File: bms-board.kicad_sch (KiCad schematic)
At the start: 1 part, among them U1 LTC6804-2

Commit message: Release/0.1 (#8)
* feat: add 6804-2 kicad symbol

* feat: add 6804-2 kicad symbol (#3)

* TEMPLATE: add pull request description template

* feat: add automated git flow setup script

* update feature/add-cells branch to latest develop edition (#4)

* feat: add 6804-2 kicad symbol

* TEMPLATE: add pull request description template

* feat: add automated git flow setup script

* update feature/our-symbol-library branch to latest develop edition (#5)

* TEMPLATE: add pull request description template

* feat: add automated git flow setup script

* feat: a maybe working fixed wing schematic symbol library

* feat: add line to checkout dev branch when running setup script

* feat: fix FixedWing symbol library to include LTC6804-2

* refactor: verifying symbol library works, remove individual ltc6804-2 symbol

* feat: adding needed files

* feat: edit conflict in setup script

* Merging new develop into new feature (#6)

* feat: add 6804-2 kicad symbol

* TEMPLATE: add pull request description template

* feat: add automated git flow setup script

* update feature/our-symbol-library branch to latest develop edition (#5)

* TEMPLATE: add pull request description template

* feat: add automated git flow setup script

* feat: a maybe working fixed wing schematic symbol library

* feat: add line to checkout dev branch when running setup script

* feat: fix FixedWing symbol library to include LTC6804-2

* refactor: verifying symbol library works, remove individual ltc6804-2 symbol

* feat: adding needed files

* feat: edit conflict in setup script

---------

Co-authored-by: Ephram Cola Jacquin <89238547+ephram2004@users.noreply.github.com>
Co-authored-by: Ephram Cola Jacquin <ecolajacquin@gmail.com>

* fix: changed symbol for easier schematic design and orginization by pin logic

* docs: Update pull_request_template.md

---------

Co-authored-by: Ephram Cola Jacquin <89238547+ephram2004@users.noreply.gith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
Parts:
- removed U1: LTC6804-2, Package_SO:SSOP-48_5.3x12.8mm_P0.5mm, symbol Battery_Management:LTC6804-2
- added U3: LTC6804-2, Package_SO:SSOP-48_5.3x12.8mm_P0.5mm, symbol FixedWing:LTC6804-2
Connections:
- new net: U3.30 (V-), U3.31 (V-)
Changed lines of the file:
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@@
 (kicad_sch (version 20230121) (generator eeschema)
   (paper "A4")
-  (symbol (lib_id "Battery_Management:LTC6804-2") (at 148.59 92.71 0) (unit 1)
+  (symbol (lib_name "LTC6804-2_1") (lib_id "FixedWing:LTC6804-2") (at 133.35 96.52 0) (unit 1)
     (in_bom yes) (on_board yes) (dnp no) (fields_autoplaced)
-    (property "Reference" "U1" (at 148.59 54.61 0)
-      (effects (font (size 1.27 1.27)))
+    (property "Reference" "U3" (at 135.5441 58.42 0)
+      (effects (font (size 1.27 1.27)) (justify left))
     )
-    (property "Value" "LTC6804-2" (at 148.59 57.15 0)
-      (effects (font (size 1.27 1.27)))
+    (property "Value" "LTC6804-2" (at 135.5441 60.96 0)
+      (effects (font (size 1.27 1.27)) (justify left))
     )
-    (property "Footprint" "Package_SO:SSOP-48_5.3x12.8mm_P0.5mm" (at 148.59 130.81 0)
+    (property "Footprint" "Package_SO:SSOP-48_5.3x12.8mm_P0.5mm" (at 133.35 133.35 0)
       (effects (font (size 1.27 1.27)) hide)
     )
-    (property "Datasheet" "https://www.analog.com/media/en/technical-documentation/data-sheets/680412fc.pdf" (at 151.13 55.88 0)
+    (property "Datasheet" "https://www.analog.com/media/en/technical-documentation/data-sheets/680412fc.pdf" (at 147.32 62.23 0)
       (effects (font (size 1.27 1.27)) hide)
     )
+    (pin "37")
+    (pin "2")
+    (pin "39")
+    (pin "32")
+    (pin "36")
+    (pin "4")
+    (pin "41")
+    (pin "11")
+    (pin "20")
+    (pin "12")
+    (pin "21")
+    (pin "30")
+    (pin "33")
+    (pin "16")
     (pin "19")
-    (pin "20")
+    (pin "34")
+    (pin "40")
+    (pin "1")
+    (pin "13")
     (pin "17")
-    (pin "21")
-    (pin "39")
-    (pin "40")
-    (pin "16")
+    (pin "10")
+    (pin "18")
+    (pin "22")
+    (pin "26")
+    (pin "23")
+    (pin "24")
+    (pin "28")
     (pin "15")
-    (pin "22")
-    (pin "12")
-    (pin "44")
+    (pin "14")
+    (pin "27")
+    (pin "25")
+    (pin "29")
+    (pin "3")
+    (pin "35")
+    (pin "31")
+    (pin "38")
+    (pin "5")
+    (pin "42")
+    (pin "43")
+    (pin "48")
+    (pin "6")
+    (pin "7")
     (pin "45")
+    (pin "8")
+    (pin "9")
     (pin "46")
     (pin "47")
-    (pin "48")
-    (pin "23")
-    (pin "4")
-    (pin "11")
-    (pin "10")
-    (pin "5")
-    (pin "6")
-    (pin "7")
-    (pin "8")
-    (pin "9")
-    (pin "1")
-    (pin "24")
-    (pin "25")
-    (pin "26")
-    (pin "27")
-    (pin "28")
-    (pin "29")
-    (pin "3")
-    (pin "30")
-    (pin "31")
-    (pin "32")
-    (pin "33")
-    (pin "34")
-    (pin "35")
-    (pin "36")
-    (pin "37")
-    (pin "38")
-    (pin "13")
-    (pin "18")
-    (pin "2")
-    (pin "14")
-    (pin "41")
-    (pin "42")
-    (pin "43")
+    (pin "44")
     (instances
       (project "bms-board"
         (path "/8a7831d1-a913-4f04-8780-225d2234b41d"
-          (reference "U1") (unit 1)
+          (reference "U3") (unit 1)
         )
       )

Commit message: feat: started adding cell nets
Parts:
- removed U3: LTC6804-2, Package_SO:SSOP-48_5.3x12.8mm_P0.5mm, symbol FixedWing:LTC6804-2
- added U1: LTC6804-2, Package_SO:SSOP-48_5.3x12.8mm_P0.5mm, symbol FixedWing:LTC6804-2
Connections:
- new net: U1.14 (C6), U1.16 (C5), U1.18 (C4)
- new net: U1.2 (C12), U1.4 (C11), U1.6 (C10)
- new net: U1.30 (V-), U1.31 (V-)
- new net C0_IN: U1.26 (C0)
- no-connect marks 0 -> 6
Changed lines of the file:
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@@
 (kicad_sch (version 20230121) (generator eeschema)
   (paper "A4")
-  (symbol (lib_name "LTC6804-2_1") (lib_id "FixedWing:LTC6804-2") (at 133.35 96.52 0) (unit 1)
+  (junction (at 158.75 62.23) (diameter 0) (color 0 0 0 0)
+  )
+  (junction (at 158.75 92.71) (diameter 0) (color 0 0 0 0)
+  )
+  (no_connect (at 154.94 64.77))
+  (no_connect (at 154.94 90.17))
+  (no_connect (at 154.94 95.25))
+  (no_connect (at 154.94 69.85))
+  (no_connect (at 154.94 100.33))
+  (no_connect (at 154.94 59.69))
+  (wire (pts (xy 154.94 57.15) (xy 158.75 57.15))
+    (stroke (width 0) (type default))
+  )
+  (wire (pts (xy 158.75 57.15) (xy 158.75 62.23))
+    (stroke (width 0) (type default))
+  )
+  (wire (pts (xy 158.75 92.71) (xy 158.75 97.79))
+    (stroke (width 0) (type default))
+  )
+  (wire (pts (xy 154.94 67.31) (xy 158.75 67.31))
+    (stroke (width 0) (type default))
+  )
+  (wire (pts (xy 154.94 62.23) (xy 158.75 62.23))
+    (stroke (width 0) (type default))
+  )
+  (wire (pts (xy 158.75 87.63) (xy 158.75 92.71))
+    (stroke (width 0) (type default))
+  )
+  (wire (pts (xy 154.94 97.79) (xy 158.75 97.79))
+    (stroke (width 0) (type default))
+  )
+  (wire (pts (xy 144.78 125.73) (xy 144.78 123.19))
+    (stroke (width 0) (type default))
+  )
+  (wire (pts (xy 154.94 92.71) (xy 158.75 92.71))
+    (stroke (width 0) (type default))
+  )
+  (wire (pts (xy 154.94 87.63) (xy 158.75 87.63))
+    (stroke (width 0) (type default))
+  )
+  (wire (pts (xy 154.94 118.11) (xy 203.2 118.11))
+    (stroke (width 0) (type default))
+  )
+  (wire (pts (xy 139.7 125.73) (xy 139.7 123.19))
+    (stroke (width 0) (type default))
+  )
+  (wire (pts (xy 158.75 62.23) (xy 158.75 67.31))
+    (stroke (width 0) (type default))
+  )
+  (wire (pts (xy 139.7 125.73) (xy 144.78 125.73))
+    (stroke (width 0) (type default))
+  )
+  (global_label "C1_IN" (shape input) (at 203.2 113.03 0) (fields_autoplaced)
+    (effects (font (size 1.27 1.27)) (justify left))
+    (property "Intersheetrefs" "${INTERSHEET_REFS}" (at 211.5676 113.03 0)
+      (effects (font (size 1.27 1.27)) (justify left) hide)
+    )
+  )
+  (global_label "C0_IN" (shape input) (at 203.2 118.11 0) (fields_autoplaced)
+    (effects (font (size 1.27 1.27)) (justify left))
+    (property "Intersheetrefs" "${INTERSHEET_REFS}" (at 211.5676 118.11 0)
+      (effects (font (size 1.27 1.27)) (justify left) hide)
+    )
+  )
+  (global_label "C2_IN" (shape input) (at 203.2 107.95 0) (fields_autoplaced)
+    (effects (font (size 1.27 1.27)) (justify left))
+    (property "Intersheetrefs" "${INTERSHEET_REFS}" (at 211.5676 107.95 0)
+      (effects (font (size 1.27 1.27)) (justify left) hide)
+    )
+  )
+  (global_label "C5_IN" (shape input) (at 203.2 82.55 0) (fields_autoplaced)
+    (effects (font (size 1.27 1.27)) (justify left))
+    (property "Intersheetrefs" "${INTERSHEET_REFS}" (at 211.5676 82.55 0)
+      (effects (font (size 1.27 1.27)) (justify left) hide)
+    )
+  )
+  (global_label "C6_IN" (shape input) (at 203.2 77.47 0) (fields_autoplaced)
+    (effects (font (size 1.27 1.27)) (justify left))
+    (property "Intersheetrefs" "${INTERSHEET_REFS}" (at 211.5676 77.47 0)
+      (effects (font (size 1.27 1.27)) (justify left) hide)
+    )
+  )
+  (global_label "C4_IN" (shape input) (at 203.2 87.63 0) (fields_autoplaced)
+    (effects (font (size 1.27 1.27)) (justify left))
+    (property "Intersheetrefs" "${INTERSHEET_REFS}" (at 211.5676 87.63 0)
+      (effects (font (size 1.27 1.27)) (justify left) hide)
+    )
+  )
+  (global_label "C7_IN" (shape input) (at 203.2 72.39 0) (fields_autoplaced)
+    (effects (font (size 1.27 1.27)) (justify left))
+    (property "Intersheetrefs" "${INTERSHEET_REFS}" (at 211.5676 72.39 0)
+      (effects (font (size 1.27 1.27)) (justify left) hide)
+    )
+  )
+  (global_label "C3_IN" (shape input) (at 203.2 102.87 0) (fields_autoplaced)
+    (effects (font (size 1.27 1.27)) (justify left))
+    (property "Intersheetrefs" "${INTERSHEET_REFS}" (at 211.5676 102.87 0)
+      (effects (font (size 1.27 1.27)) (justify left) hide)
+    )
+  )
+  (symbol (lib_name "LTC6804-2_1") (lib_id "FixedWing:LTC6804-2") (at 142.24 87.63 0) (unit 1)
     (in_bom yes) (on_board yes) (dnp no) (fields_autoplaced)
-    (property "Reference" "U3" (at 135.5441 58.42 0)
+    (property "Reference" "U1" (at 144.4341 49.53 0)
       (effects (font (size 1.27 1.27)) (justify left))
     )
-    (property "Value" "LTC6804-2" (at 135.5441 60.96 0)
+    (property "Value" "LTC6804-2" (at 144.4341 52.07 0)
       (effects (font (size 1.27 1.27)) (justify left))
     )
-    (property "Footprint" "Package_SO:SSOP-48_5.3x12.8mm_P0.5mm" (at 133.35 133.35 0)
+    (property "Footprint" "Package_SO:SSOP-48_5.3x12.8mm_P0.5mm" (at 142.24 124.46 0)
       (effects (font (size 1.27 1.27)) hide)
     )
-    (property "Datasheet" "https://www.analog.com/media/en/technical-documentation/data-sheets/680412fc.pdf" (at 147.32 62.23 0)
+    (property "Datasheet" "https://www.analog.com/media/en/technical-documentation/data-sheets/680412fc.pdf" (at 156.21 53.34 0)
       (effects (font (size 1.27 1.27)) hide)
     )
+    (pin "31")
+    (pin "36")
     (pin "37")
+    (pin "18")
+    (pin "48")
+    (pin "5")
+    (pin "6")
+    (pin "23")
+    (pin "1")
+    (pin "34")
+    (pin "10")
+    (pin "26")
+    (pin "22")
+    (pin "29")
+    (pin "32")
+    (pin "14")
+    (pin "16")
     (pin "2")
+    (pin "44")
+    (pin "11")
+    (pin "42")
+    (pin "7")
+    (pin "8")
+    (pin "9")
+    (pin "17")
+    (pin "24")
     (pin "39")
-    (pin "32")
-    (pin "36")
-    (pin "4")
-    (pin "41")
-    (pin "11")
+    (pin "21")
+    (pin "43")
+    (pin "19")
+    (pin "40")
+    (pin "35")
+    (pin "30")
+    (pin "45")
+    (pin "15")
+    (pin "25")
+    (pin "28")
+    (pin "46")
+    (pin "38")
     (pin "20")
     (pin "12")
-    (pin "21")
-    (pin "30")
+    (pin "3")
+    (pin "41")
+    (pin "4")
     (pin "33")
-    (pin "16")
-    (pin "19")
-    (pin "34")
-    (pin "40")
-    (pin "1")
     (pin "13")
-    (pin "17")
-    (pin "10")
-    (pin "18")
-    (pin "22")
-    (pin "26")
-    (pin "23")
-    (pin "24")
-    (pin "28")
-    (pin "15")
-    (pin "14")
     (pin "27")
-    (pin "25")
-    (pin "29")
-    (pin "3")
-    (pin "35")
-    (pin "31")
-    (pin "38")
-    (pin "5")
-    (pin "42")
-    (pin "43")
-    (pin "48")
-    (pin "6")
-    (pin "7")
-    (pin "45")
-    (pin "8")
-    (pin "9")
-    (pin "46")
     (pin "47")
-    (pin "44")
     (instances
       (project "bms-board"
         (path "/8a7831d1-a913-4f04-8780-225d2234b41d"
-          (reference "U3") (unit 1)
+          (reference "U1") (unit 1)
         )
       )

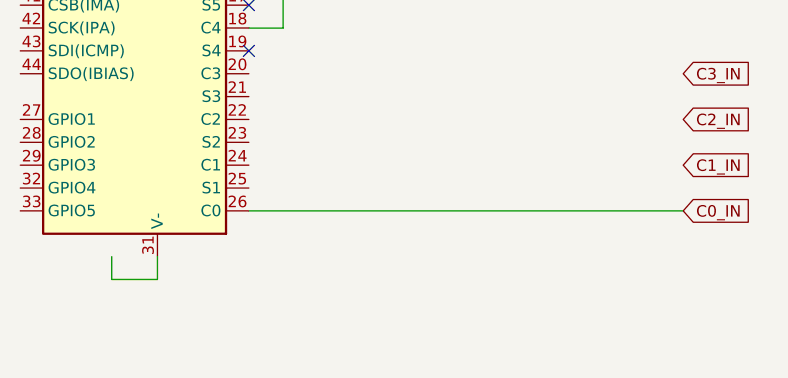
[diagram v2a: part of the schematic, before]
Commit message: feat: still some more LTC6804-2 symbol edits
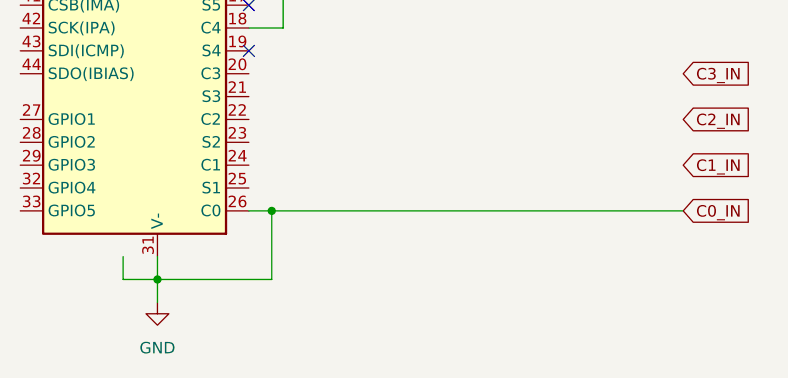
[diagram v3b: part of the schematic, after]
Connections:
- net C0_IN is gone; now on net GND: U1.26 (C0)
- net GND: now reaches U1.30 (V-), U1.31 (V-)
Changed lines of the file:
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@@
   (junction (at 158.75 62.23) (diameter 0) (color 0 0 0 0)
   )
+  (junction (at 157.48 118.11) (diameter 0) (color 0 0 0 0)
+  )
   (junction (at 158.75 92.71) (diameter 0) (color 0 0 0 0)
+  )
+  (junction (at 144.78 125.73) (diameter 0) (color 0 0 0 0)
   )
   (no_connect (at 154.94 64.77))
@@
     (stroke (width 0) (type default))
   )
+  (wire (pts (xy 144.78 128.27) (xy 144.78 125.73))
+    (stroke (width 0) (type default))
+  )
+  (wire (pts (xy 157.48 118.11) (xy 203.2 118.11))
+    (stroke (width 0) (type default))
+  )
   (wire (pts (xy 158.75 57.15) (xy 158.75 62.23))
     (stroke (width 0) (type default))
@@
     (stroke (width 0) (type default))
   )
+  (wire (pts (xy 144.78 125.73) (xy 157.48 125.73))
+    (stroke (width 0) (type default))
+  )
   (wire (pts (xy 154.94 67.31) (xy 158.75 67.31))
     (stroke (width 0) (type default))
@@
     (stroke (width 0) (type default))
   )
-  (wire (pts (xy 154.94 118.11) (xy 203.2 118.11))
-    (stroke (width 0) (type default))
-  )
-  (wire (pts (xy 139.7 125.73) (xy 139.7 123.19))
+  (wire (pts (xy 154.94 118.11) (xy 157.48 118.11))
+    (stroke (width 0) (type default))
+  )
+  (wire (pts (xy 140.97 125.73) (xy 140.97 123.19))
     (stroke (width 0) (type default))
   )
@@
     (stroke (width 0) (type default))
   )
-  (wire (pts (xy 139.7 125.73) (xy 144.78 125.73))
+  (wire (pts (xy 157.48 118.11) (xy 157.48 125.73))
+    (stroke (width 0) (type default))
+  )
+  (wire (pts (xy 140.97 125.73) (xy 144.78 125.73))
     (stroke (width 0) (type default))
   )
@@
         )
       )
+    )
+  )
+  (symbol (lib_id "power:GND") (at 144.78 128.27 0) (unit 1)
+    (in_bom yes) (on_board yes) (dnp no) (fields_autoplaced)
+    (property "Reference" "#PWR01" (at 144.78 134.62 0)
+      (effects (font (size 1.27 1.27)) hide)
+    )
+    (property "Value" "GND" (at 144.78 133.35 0)
+      (effects (font (size 1.27 1.27)))
+    )
+    (property "Footprint" "" (at 144.78 128.27 0)
+      (effects (font (size 1.27 1.27)) hide)
+    )
+    (property "Datasheet" "" (at 144.78 128.27 0)
+      (effects (font (size 1.27 1.27)) hide)
+    )
+    (pin "1")
+    (instances
+      (project "bms-board"
+        (path "/8a7831d1-a913-4f04-8780-225d2234b41d"
+          (reference "#PWR01") (unit 1)
+        )
+      )
